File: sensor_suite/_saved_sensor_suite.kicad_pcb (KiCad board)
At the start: 4 copper layers, 78.9 x 74.1 mm, 14 parts, among them CN1 609-3634-ND, J1 Bar02, J2 Conn_02x10_Counter_Clockwise, J3 Conn_01x02, J4 Conn_01x02, J5 LSM303, J6 Conn_02x20_Counter_Clockwise, U1 MAX6581, U2 LM3480-3.3

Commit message: Sensor Suite is finally buttoned up
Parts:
- added C10: 100 pF, Capacitor_SMD:C_0805_2012Metric_Pad1.15x1.40mm_HandSolder, F.Cu at (160.1, 105.0)
- added C6: 100 pF, Capacitor_SMD:C_0805_2012Metric_Pad1.15x1.40mm_HandSolder, F.Cu at (173.1, 99.3)
- added C7: 100 pF, Capacitor_SMD:C_0805_2012Metric_Pad1.15x1.40mm_HandSolder, F.Cu at (160.9, 100.8)
- added C8: 100 pF, Capacitor_SMD:C_0805_2012Metric_Pad1.15x1.40mm_HandSolder, F.Cu at (164.9, 110.0)
- added C9: 100 pF, Capacitor_SMD:C_0805_2012Metric_Pad1.15x1.40mm_HandSolder, F.Cu at (160.7, 109.2)
- added JP1: SolderJumper_3_Open, Jumper:SolderJumper-3_P1.3mm_Open_RoundedPad1.0x1.5mm_NumberLabels, F.Cu at (174.5, 134.0)
- added JP2: SolderJumper_3_Open, Jumper:SolderJumper-3_P1.3mm_Open_RoundedPad1.0x1.5mm_NumberLabels, F.Cu at (180.0, 134.0)
- added JP3: SolderJumper_3_Open, Jumper:SolderJumper-3_P1.3mm_Open_RoundedPad1.0x1.5mm_NumberLabels, F.Cu at (168.4, 134.0)
- added JP4: SolderJumper_3_Open, Jumper:SolderJumper-3_P1.3mm_Open_RoundedPad1.0x1.5mm_NumberLabels, F.Cu at (162.9, 134.0)
- added R1: 10k, Resistor_SMD:R_0805_2012Metric_Pad1.15x1.40mm_HandSolder, F.Cu at (192.8, 85.2)
- added R2: 10k, Resistor_SMD:R_0805_2012Metric_Pad1.15x1.40mm_HandSolder, F.Cu at (191.8, 89.0)
- added U3: Pi3+, ROV:Pi3+, F.Cu at (187.2, 133.0)
- U1: footprint Package_DFN_QFN:QFN-20-1EP_5x5mm_P0.65mm_EP3.35x3.35mm -> Package_DFN_QFN:QFN-24-1EP_4x4mm_P0.5mm_EP2.7x2.7mm
- moved C3 14.4 mm to (162.2, 97.1), turned to 90 degrees
- moved C2 7.07 mm to (167.2, 90.9), turned to 90 degrees
- moved C1 5.64 mm to (171.1, 94.8)
- moved J1 4.78 mm to (154.9, 98.2)
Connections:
- C3 pad 1: +3V3 -> Net-(C3-Pad1)
- CN1 pad A2: PWM_4 -> +5VP
- CN1 pad A3: +5VP -> PWM_4
- CN1 pad A4: Net-(CN1-PadA4) -> /DigitalOutput1
- CN1 pad B2: PWM_5 -> +5VP
- CN1 pad B3: +5VP -> PWM_5
- CN1 pad B4: Net-(CN1-PadB4) -> /DigitalOutput2
- CN1 pad C1: PWM_2 -> SDA_iso
- CN1 pad C2: PWM_6 -> +5VP
- CN1 pad C3: +5VP -> PWM_6
- CN1 pad C4: /SDA_iso -> PWM_2
- CN1 pad D1: PWM_3 -> SCL_iso
- CN1 pad D2: PWM_7 -> +5VP
- CN1 pad D3: +5VP -> PWM_7
- CN1 pad D4: /SCL_iso -> PWM_3
- J1 pad 2: /SCL_iso -> SCL_iso
- J1 pad 3: /SDA_iso -> SDA_iso
- J2 pad 18: /SCL_iso -> SCL_iso
- J2 pad 19: /SDA_iso -> SDA_iso
- J5 pad 1: /SCL_iso -> SDA_iso
- J5 pad 2: /SDA_iso -> SCL_iso
- J6 pad 11: Net-(J6-Pad11) -> /DigitalOutput1
- J6 pad 13: Net-(J6-Pad13) -> /DigitalOutput2
- J6 pad 29: Net-(J6-Pad29) -> DigitalOutput3
- J6 pad 3: /SDA_iso -> SDA_iso
- J6 pad 31: Net-(J6-Pad31) -> DigitalOutput4
- J6 pad 33: Net-(J6-Pad33) -> DigitalOutput6
- J6 pad 35: Net-(J6-Pad35) -> DigitalOutput5
- J6 pad 5: /SCL_iso -> SCL_iso
- U1 pad 1: /temp1n -> /temp1p
- U1 pad 10: (no net) -> Net-(C9-Pad1)
- U1 pad 11: (no net) -> Net-(C9-Pad2)
- U1 pad 12: (no net) -> Net-(C8-Pad1)
- U1 pad 13: (no net) -> Net-(C8-Pad2)
- U1 pad 14: (no net) -> +5VP
- U1 pad 15: (no net) -> +5VP
- U1 pad 16: (no net) -> Net-(U1-Pad16)
- U1 pad 17: +3V3 -> +5VP
- U1 pad 18: (no net) -> Net-(U1-Pad18)
- U1 pad 19: /SCL_iso -> SDA_iso
- U1 pad 2: /temp1p -> /temp1n
- U1 pad 20: /SDA_iso -> SCL_iso
- U1 pad 21: GNDS -> Net-(C3-Pad1)
- U1 pad 3: /temp2n -> /temp2p
- U1 pad 4: /temp2p -> /temp2n
- U1 pad 5: (no net) -> Net-(C7-Pad2)
- U1 pad 6: (no net) -> Net-(U1-Pad6)
- U1 pad 7: (no net) -> Net-(C7-Pad1)
- U1 pad 8: (no net) -> Net-(C10-Pad1)
- U1 pad 9: (no net) -> Net-(C10-Pad2)
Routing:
- net /SDA_iso: track 263.6 -> 0.00 mm
- net /SCL_iso: track 256.9 -> 0.00 mm, vias 2 -> 0
- net SDA_iso: track 0.00 -> 214.8 mm
- net SCL_iso: track 0.00 -> 200.7 mm, vias 0 -> 3
- net /DigitalOutput2: track 0.00 -> 112.7 mm, vias 0 -> 1
- net /DigitalOutput1: track 0.00 -> 104.9 mm, vias 0 -> 1
- net DigitalOutput3: track 0.00 -> 43.2 mm, vias 0 -> 1
- net DigitalOutput4: track 0.00 -> 43.0 mm, vias 0 -> 1
- net DigitalOutput6: track 0.00 -> 36.3 mm, vias 0 -> 1
- net DigitalOutput5: track 0.00 -> 29.7 mm, vias 0 -> 1
- net Net-(C3-Pad1): track 0.00 -> 25.5 mm, vias 0 -> 2
- net PWM_13: track 45.1 -> 67.8 mm
- net PWM_14: track 46.2 -> 63.0 mm
- net +3V3: track 99.1 -> 82.8 mm
- net /temp2p: track 17.7 -> 31.5 mm
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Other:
- board size 78.9 x 74.1 mm -> 79 x 82.5 mm
- net class Default: trace_width 0.25 -> 0.2286

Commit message: sensor board
sensor board push
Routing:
- net /DigitalOutput2: track 112.7 -> 111.0 mm
- net PWM_12: track 72.7 -> 73.7 mm

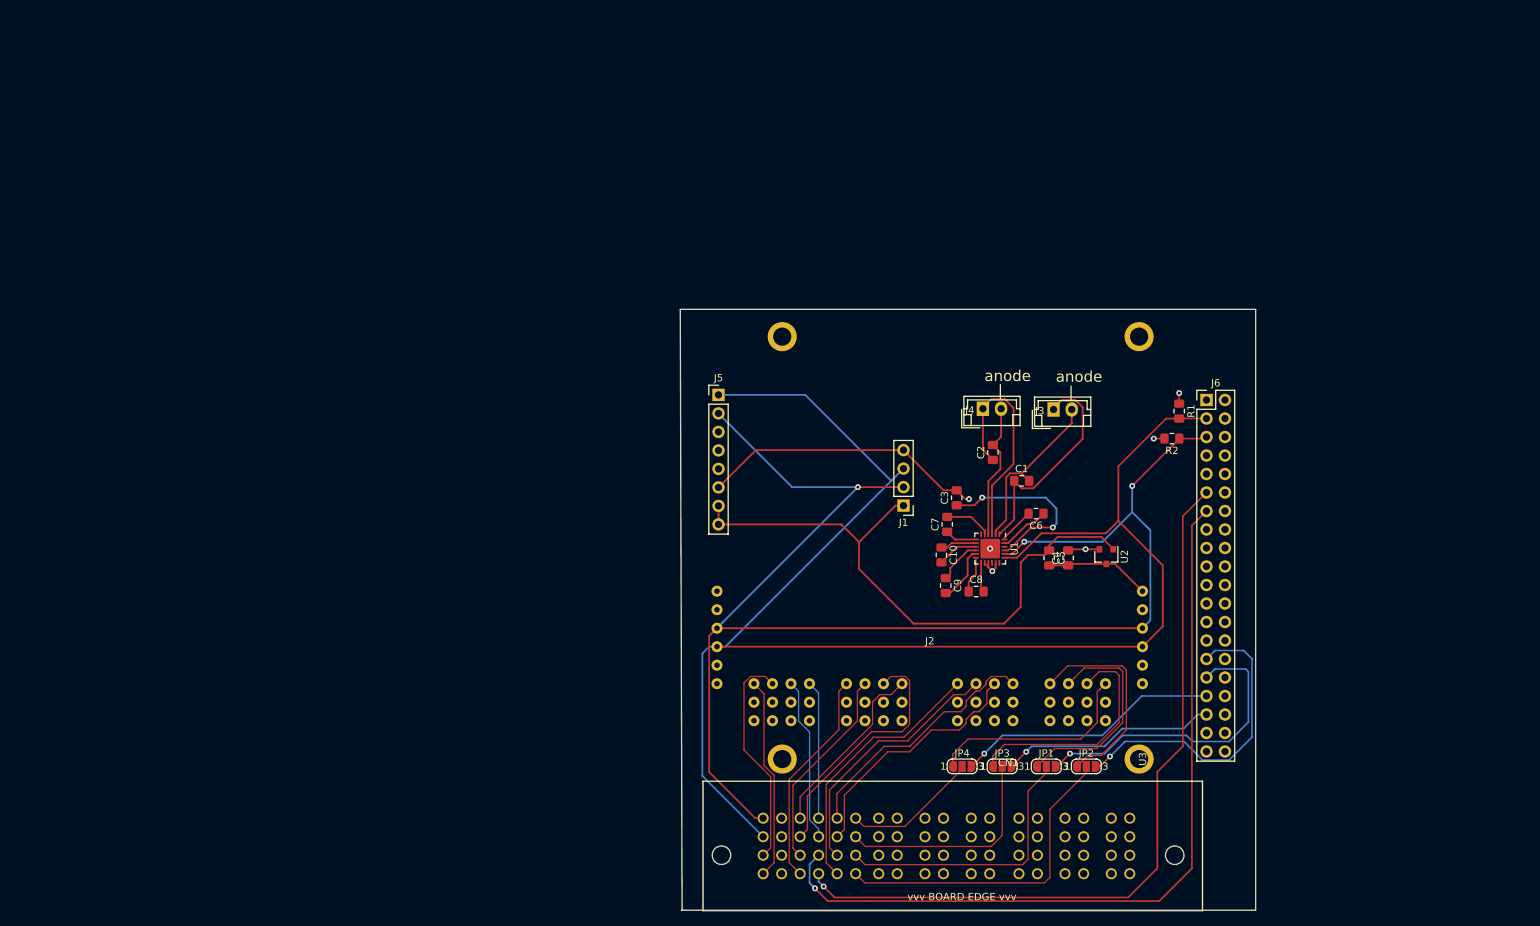
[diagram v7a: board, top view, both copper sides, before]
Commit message: Sensor Board with Video Driver
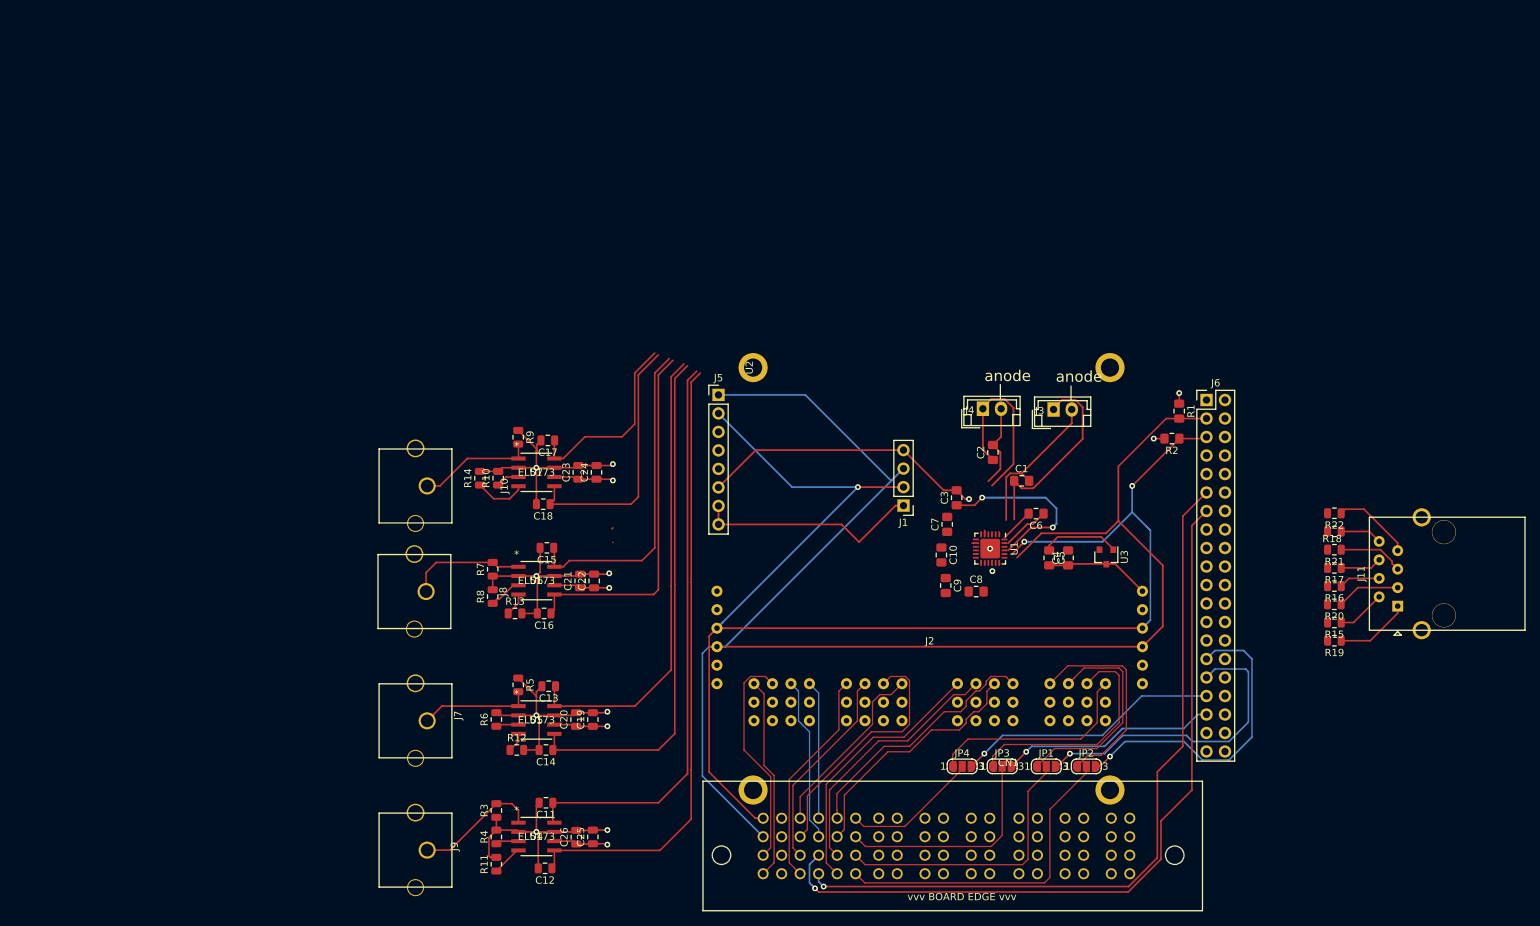
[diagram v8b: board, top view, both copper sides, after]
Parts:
- added C11: 1 pF, Capacitor_SMD:C_0805_2012Metric, F.Cu at (105.8, 139.0)
- added C12: 1 pF, Capacitor_SMD:C_0805_2012Metric, F.Cu at (105.7, 148.0)
- added C13: 1 pF, Capacitor_SMD:C_0805_2012Metric, F.Cu at (106.2, 123.0)
- added C14: 1 pF, Capacitor_SMD:C_0805_2012Metric, F.Cu at (105.8, 131.8)
- added C15: 1 pF, Capacitor_SMD:C_0805_2012Metric, F.Cu at (105.9, 104.0)
- added C16: 1 pF, Capacitor_SMD:C_0805_2012Metric, F.Cu at (105.6, 113.0)
- added C17: 1 pF, Capacitor_SMD:C_0805_2012Metric, F.Cu at (106.1, 89.2)
- added C18: 1 pF, Capacitor_SMD:C_0805_2012Metric, F.Cu at (105.4, 98.0)
- added C19: 4.7 uF, Capacitor_SMD:C_0805_2012Metric, F.Cu at (112.2, 127.6)
- added C20: 0.1 uF, Capacitor_SMD:C_0805_2012Metric, F.Cu at (109.9, 127.6)
- added C21: 4.7 uF, Capacitor_SMD:C_0805_2012Metric, F.Cu at (110.5, 108.5)
- added C22: 0.1 uF, Capacitor_SMD:C_0805_2012Metric, F.Cu at (112.4, 108.5)
- added C23: 4.7 uF, Capacitor_SMD:C_0805_2012Metric, F.Cu at (110.2, 93.6)
- added C24: 0.1 uF, Capacitor_SMD:C_0805_2012Metric, F.Cu at (112.8, 93.6)
- added C25: 4.7 uF, Capacitor_SMD:C_0805_2012Metric, F.Cu at (112.2, 143.7)
- added C26: 0.1 uF, Capacitor_SMD:C_0805_2012Metric, F.Cu at (110.0, 143.7)
- added J10: Conn_01x01, ROV:RCA_Jack, F.Cu at (87.9, 95.5)
- added J11: RJ45, ROV:RJ45_Amphenol_54602-x08_Horizontal, F.Cu at (222.8, 112.0)
- added J7: Conn_01x01, ROV:RCA_Jack, F.Cu at (87.9, 127.8)
- added J8: Conn_01x01, ROV:RCA_Jack, F.Cu at (87.8, 110.0)
- added J9: Conn_01x01, ROV:RCA_Jack, F.Cu at (87.9, 145.5)
- added R10: 50, Resistor_SMD:R_0805_2012Metric, F.Cu at (99.2, 94.4)
- added R11: 50, Resistor_SMD:R_0805_2012Metric, F.Cu at (99.0, 147.4)
- added R12: 50, Resistor_SMD:R_0805_2012Metric, F.Cu at (101.8, 131.8)
- added R13: 50, Resistor_SMD:R_0805_2012Metric, F.Cu at (101.6, 113.0)
- added R14: 50, Resistor_SMD:R_0805_2012Metric, F.Cu at (96.8, 94.4)
- added R15: 50, Resistor_SMD:R_0805_2012Metric, F.Cu at (214.1, 114.2)
- added R16: 50, Resistor_SMD:R_0805_2012Metric, F.Cu at (214.1, 109.2)
- added R17: 50, Resistor_SMD:R_0805_2012Metric, F.Cu at (214.1, 106.8)
- added R18: 50, Resistor_SMD:R_0805_2012Metric, F.Cu at (214.1, 101.8)
- added R19: 50, Resistor_SMD:R_0805_2012Metric, F.Cu at (214.1, 116.8)
- added R20: 50, Resistor_SMD:R_0805_2012Metric, F.Cu at (214.0, 111.8)
- added R21: 50, Resistor_SMD:R_0805_2012Metric, F.Cu at (214.1, 104.2)
- added R22: 50, Resistor_SMD:R_0805_2012Metric, F.Cu at (214.1, 99.2)
- added R3: 50, Resistor_SMD:R_0805_2012Metric, F.Cu at (99.0, 140.1)
- added R4: 50, Resistor_SMD:R_0805_2012Metric, F.Cu at (99.0, 143.7)
- added R5: 50, Resistor_SMD:R_0805_2012Metric, F.Cu at (102.0, 122.8)
- added R6: 50, Resistor_SMD:R_0805_2012Metric, F.Cu at (99.0, 127.6)
- added R7: 50, Resistor_SMD:R_0805_2012Metric, F.Cu at (98.5, 106.9)
- added R8: 50, Resistor_SMD:R_0805_2012Metric, F.Cu at (98.5, 110.7)
- added R9: 50, Resistor_SMD:R_0805_2012Metric, F.Cu at (102.0, 88.8)
- added U4: EL5173, ROV:EL5173ISZ, F.Cu at (104.5, 143.6)
- added U5: EL5173, ROV:EL5173ISZ, F.Cu at (104.5, 127.6)
- added U6: EL5173, ROV:EL5173ISZ, F.Cu at (104.5, 108.5)
- added U7: EL5173, ROV:EL5173ISZ, F.Cu at (104.5, 93.6)
- C10, C9: value 100 pF -> 0.1uF
- C4, C5: value 0.1uF -> 100 pF
- U2: value LM3480-3.3 -> Pi3+; footprint Package_TO_SOT_SMD:SOT-23 -> ROV:Pi3+
- U3: value Pi3+ -> LM3480-3.3; footprint ROV:Pi3+ -> Package_TO_SOT_SMD:SOT-23
- moved U2 55.0 mm to (134.2, 79.2)
- moved U3 28.1 mm to (182.8, 105.2), turned to 270 degrees
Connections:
- C10 pad 1: Net-(C10-Pad1) -> +3V3
- C10 pad 2: Net-(C10-Pad2) -> GNDPWR
- C3 pad 2: GNDS -> GNDPWR
- C4 pad 1: GNDPWR -> Net-(C4-Pad1)
- C4 pad 2: +5VP -> Net-(C4-Pad2)
- C5 pad 1: +3V3 -> Net-(C5-Pad1)
- C5 pad 2: GNDPWR -> Net-(C5-Pad2)
- C9 pad 1: Net-(C9-Pad1) -> GNDPWR
- C9 pad 2: Net-(C9-Pad2) -> +5VP
- J1 pad 4: GNDS -> GNDPWR
- J5 pad 6: GNDS -> GNDPWR
- U1 pad 10: Net-(C9-Pad1) -> Net-(C7-Pad1)
- U1 pad 11: Net-(C9-Pad2) -> Net-(C7-Pad2)
- U1 pad 12: Net-(C8-Pad1) -> Net-(C6-Pad1)
- U1 pad 13: Net-(C8-Pad2) -> Net-(C6-Pad2)
- U1 pad 23: Net-(C6-Pad1) -> Net-(C4-Pad1)
- U1 pad 24: Net-(C6-Pad2) -> Net-(C4-Pad2)
- U1 pad 5: Net-(C7-Pad2) -> Net-(C5-Pad2)
- U1 pad 7: Net-(C7-Pad1) -> Net-(C5-Pad1)
- U1 pad 8: Net-(C10-Pad1) -> Net-(C8-Pad1)
- U1 pad 9: Net-(C10-Pad2) -> Net-(C8-Pad2)
- U2 pad 1: +3V3 -> (no net)
- U2 pad 2: +5VP -> (no net)
- U2 pad 3: GNDPWR -> (no net)
- U3 pad 1: (no net) -> +3V3
- U3 pad 2: (no net) -> +5VP
- U3 pad 3: (no net) -> GNDPWR
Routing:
- net GNDPWR: track 14.6 -> 177.0 mm, vias 1 -> 10
- net Net-(C12-Pad1): track 0.00 -> 84.9 mm
- net Net-(C11-Pad1): track 0.00 -> 78.7 mm
- net Net-(C14-Pad1): track 0.00 -> 71.2 mm
- net Net-(C13-Pad1): track 0.00 -> 63.6 mm
- net Net-(C16-Pad1): track 0.00 -> 49.7 mm
- net Net-(C15-Pad1): track 0.00 -> 44.3 mm
- net +3V3: track 82.8 -> 42.1 mm
- net GNDS: track 39.3 -> 0.00 mm, vias 1 -> 0
- net Net-(C18-Pad1): track 0.00 -> 35.9 mm
- net Net-(C17-Pad1): track 0.00 -> 26.4 mm
- net +5VP: track 11.5 -> 33.8 mm, vias 4 -> 7
- net Net-(J9-Pad1): track 0.00 -> 17.2 mm
- net Net-(J8-Pad1): track 0.00 -> 16.1 mm
- net Net-(J10-Pad1): track 0.00 -> 16.1 mm
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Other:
- board outline removed
